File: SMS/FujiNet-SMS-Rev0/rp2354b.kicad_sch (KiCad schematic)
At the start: 46 parts, among them J2 DBG UART, Q1 2N7002, SW1 RESET, SW2 BOOTSEL, U1 RP2354B, Y1 12MHz

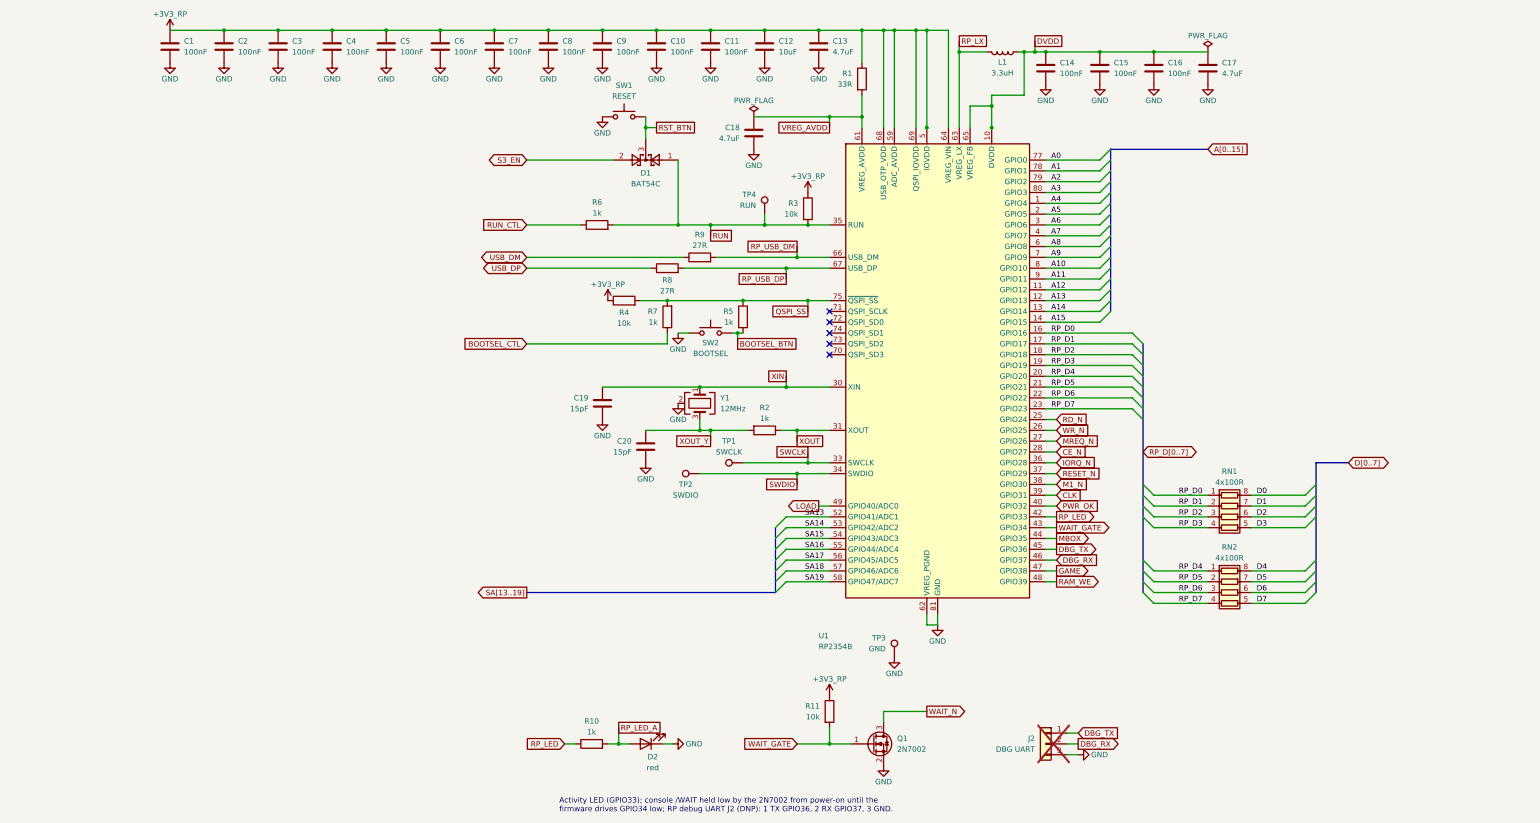
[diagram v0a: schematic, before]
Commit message: SMS Rev0: audit with kicad-happy + datasheets, fix the edge, redraw the schematic
Edge connector: every source (SMS Power slot diagram, little-scale, a 171-5519
scan, raphnet, the barbeque and reidrac footprints) puts the EVEN pins on the
component / label side with pins 1/2 at the right.  The schematic-only
footprint had the faces swapped, which would have put console +5V on /WR.
make_edge_fp.py now writes even pads on F.Cu, odd on B.Cu, 1.75 x 8.75 mm
fingers 0.75-9.5 mm from the edge on a 65.8 mm tab; check_nets.py asserts it
and tools/audit/edge_orientation.py checks it against the sources.

kicad-happy + datasheet audit (docs/design-review-rev0.md Part 1, 27 deep
review findings, gate 27/27): R_VBPD 4.7k VBUS pull-down (SS34 leakage lifts
the P-FET gate), /WAIT gate pull-up 10k -> 4.7k (GPIO34's reset pull-down vs
the 2N7002's 2.5 V threshold), 10 uF bulk on the console 5V.

Schematic: hierarchical sheets wired on a root block diagram (edge -> RP2354B
-> ESP32-S3 -> USB, glue and SRAM under the RP, power below); every sheet
drawn left to right, the glue as a wired logic network by gate depth, the
RP2354B mirrored so its bus faces the console, small sheets on A4.  Parts
are addressed by key (design.py), no more NES reference aliasing.  sch_draw
gains hierarchical labels, sheet blocks, a bus graph and flag / power-pin
lints; gen_sch checks the hierarchy against design.py and names nets by
their last path element (one bus vector per bus: KiCad joins differing
vectors by position).  ERC 0, check_nets 437/437, check_glue 8192/8192.

JLC CPL rotations measured against the EasyEDA footprint of every LCSC part
(tools/audit/jlc); the AS6C4008 has no EasyEDA footprint.

Co-Authored-By: Claude Opus 5.5 <noreply@anthropic.com>
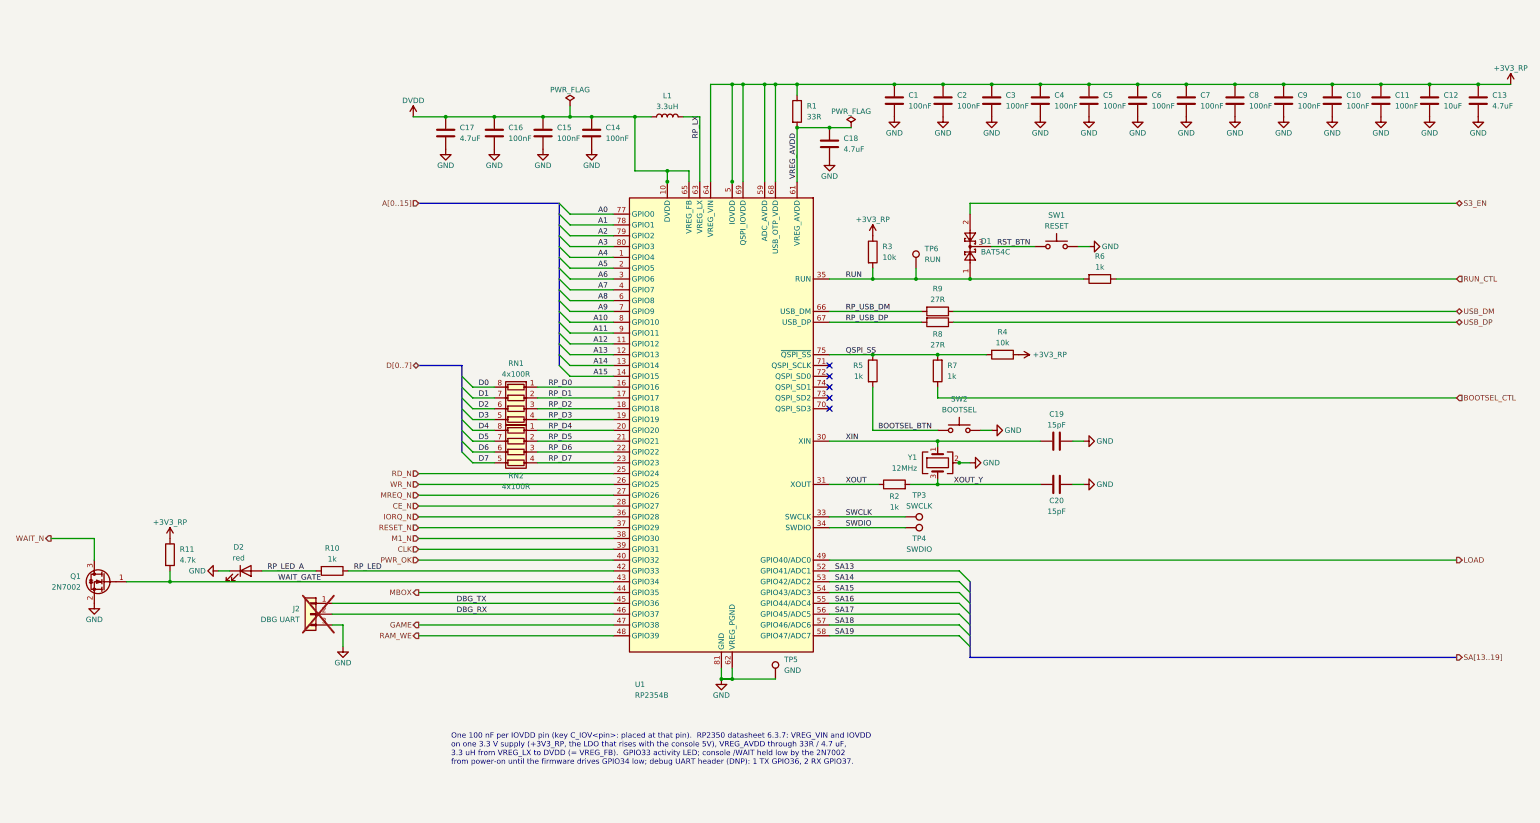
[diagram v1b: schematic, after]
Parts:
- removed TP1: SWCLK, FujiNet-SMS:TestPoint_Pad_D1.5mm, symbol Connector:TestPoint
- removed TP2: SWDIO, FujiNet-SMS:TestPoint_Pad_D1.5mm, symbol Connector:TestPoint
- added TP5: GND, FujiNet-SMS:TestPoint_Pad_D1.5mm, symbol Connector:TestPoint
- added TP6: RUN, FujiNet-SMS:TestPoint_Pad_D1.5mm, symbol Connector:TestPoint
- R11: value 10k -> 4.7k; LCSC C25804 -> C23162; MPN 0603WAF1002T5E -> 0603WAF4701T5E
- TP3: value GND -> SWCLK
- TP4: value RUN -> SWDIO
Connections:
- net GND: now also TP5.1; no longer TP3.1
- net RUN: now also TP6.1; no longer TP4.1
- net SWCLK: now also TP3.1
- net SWDIO: now also TP4.1
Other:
- note added: "One 100 nF per IOVDD pin (key C_IOV<pin>: placed at that pin). RP2350 datasheet 6.3.7: VREG_VIN and IOVDD on one 3.3 V supply (+3V3_RP, the LDO that rises with the console 5V), VREG_AVDD through 33R / 4.7 uF, 3.3 uH from VREG_LX to DVDD (= VREG_FB). GPIO33 activity LED; console /WAIT held low by the 2N7002 from power-on until the firmware drives GPIO34 low; debug UART header (DNP): 1 TX GPIO36, 2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"
- note removed: "Activity LED (GPIO33); console /WAIT held low by the 2N7002 from power-on until the firmware drives GPIO34 low; RP debug UART J2 (DNP): 1 TX GPIO36, 2 RX GPIO37, 3 GND."
- moved on the sheet: C1, C10, C11, C12, C13, C14, C15, C16, C17, C18, C19, C2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

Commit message: SMS Rev0 v2: port the FujiNet-7800 tooling, swap the near-stock-out parts
- export.py: JLCPCB and PCBWay packages (PCBWay turnkey BOM, centroid,
  assembly drawing); Manufacturer on every BOM part (design.MFR), written
  to symbols and footprints alike
- edge_geom.py: the SMS edge constants in one place (make_edge_fp,
  gen_pcb, check_gerbers); gen_pcb's body height, holes and In4 split now
  come from placement.py
- footprint paths from the schematic netlist (gen_pcb.fp_sheet_unit), so
  a part's units can be drawn on several sheets (prototype 2026-10-08:
  kicad-cli files it under the first sheet, parity accepts it)
- check_vias, check_gerbers, make_happy_config, stitch_gnd second ring,
  set_models main(), route_board.sh 12 passes / hybrid, DRC at all
  severities
- TL3342 -> TS-1187A-B-A-B (C318884), WS2812B-2020-V6 -> WS2812C-2020-V1
  (C2976072): ~5 in stock on 2026-10-07

Co-Authored-By: Claude Opus 5.5 <noreply@anthropic.com>
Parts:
- C1, C10, C11, C14, C15, C16, C2, C3, C4, C5, C6, C7, C8, C9: Manufacturer (none) -> YAGEO
- C12, C13, C17, C18, C19, C20: Manufacturer (none) -> Samsung Electro-Mechanics
- D1: Manufacturer (none) -> Nexperia
- D2: Manufacturer (none) -> Hubei KENTO Elec
- J2: Manufacturer (none) -> XFCN
- L1, Y1: Manufacturer (none) -> Abracon
- Q1: Manufacturer (none) -> Jiangsu Changjing (JSCJ)
- R1, R10, R11, R2, R3, R4, R5, R6, R7, R8, R9, RN1, RN2: Manufacturer (none) -> UNI-ROYAL
- SW1, SW2: footprint FujiNet-SMS:SW_SPST_TL3342 -> FujiNet-SMS:SW_SPST_TS-1187A; LCSC C2886898 -> C318884; MPN TL3342F160QG -> TS-1187A-B-A-B; Manufacturer (none) -> XKB Connection
- U1: Manufacturer (none) -> Raspberry Pi
